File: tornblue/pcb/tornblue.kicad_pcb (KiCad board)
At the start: 2 copper layers, 152.7 x 207.8 mm, 164 parts, among them J1 BATT, J10 USB C - USB2.0, J2 SWD, J3 BREAKOUT, J4 USB C - USB2.0, J5 BATT_PIN, J6 BATT, J7 BATT_PIN, J8 BREAKOUT, J9 SWD, Q1 AO3401A, Q2 AO3401A, Q3 AO3401A, Q4 AO3401A, SW1 SW_Push, SW10 SW_Push, SW11 SW_Push, SW12 SW_Push, SW13 SW_Push, SW14 SW_Push, SW15 SW_Push, SW16 SW_Push, SW17 SW_Push, SW18 SW_Push, SW19 EC11, SW2 SW_Push, SW20 SW_Push, SW21 SW_Push, SW22 EC11, SW23 RESET, SW24 SW_SPST, SW25 SW_Push, SW26 SW_Push, SW27 SW_Push, SW28 SW_Push, SW29 SW_Push, SW3 SW_Push, SW30 SW_Push, SW31 SW_Push, SW32 SW_Push, SW33 SW_Push, SW34 SW_Push, SW35 SW_Push, SW36 SW_Push, SW37 SW_Push, SW38 SW_Push, SW39 SW_Push, SW4 SW_Push, SW40 SW_Push, SW41 SW_Push, SW42 SW_Push, SW43 EC11, SW44 SW_Push, SW45 SW_Push, SW46 EC11, SW47 SW_SPST, SW48 RESET, SW5 SW_Push, SW6 SW_Push, SW7 SW_Push, SW8 SW_Push, SW9 SW_Push, U1 XC6220, U2 TP4056, U3 nRF52840_holyiot_18010, U4 SRV05-4, U5 TP4056, U6 XC6220, U7 SRV05-4, U8 nRF52840_holyiot_18010

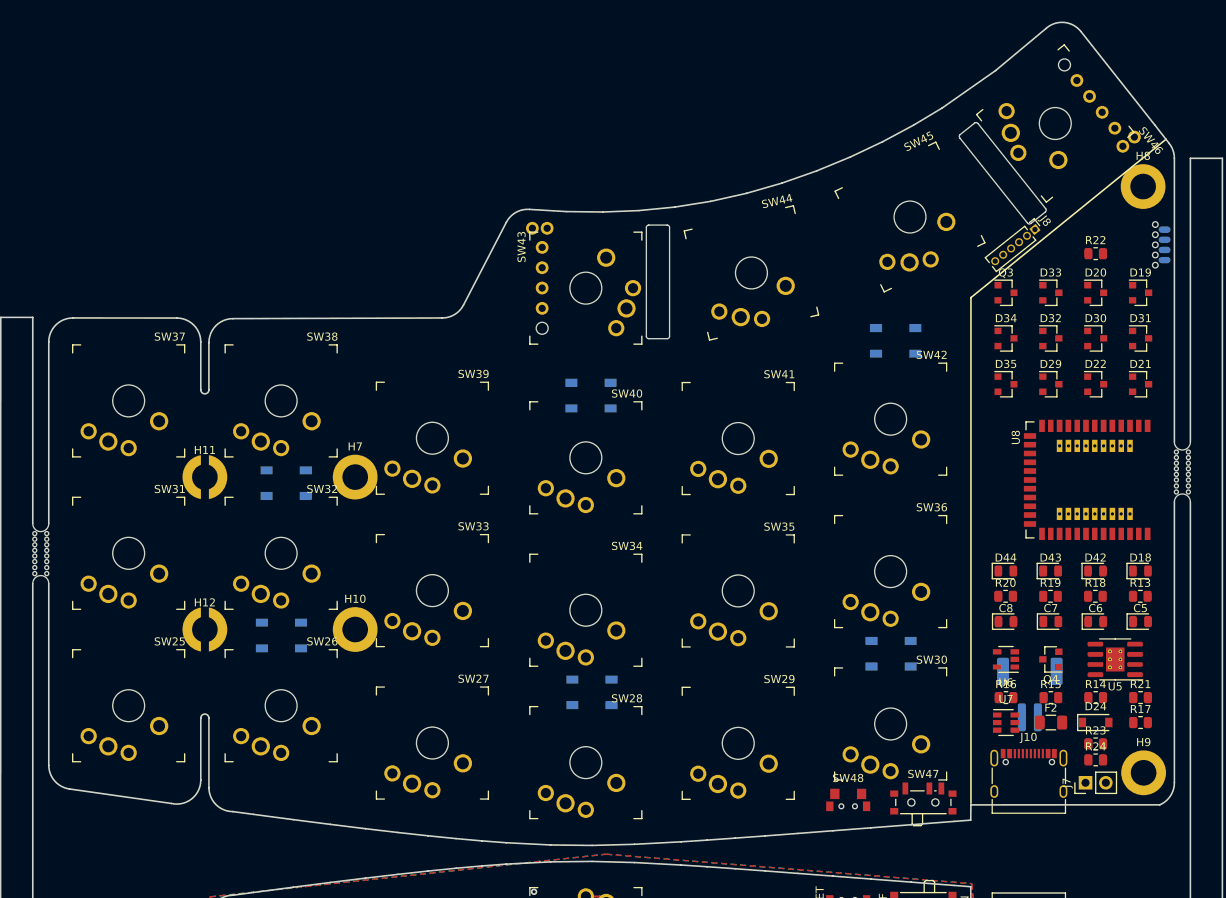
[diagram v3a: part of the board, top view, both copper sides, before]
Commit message: Add zones
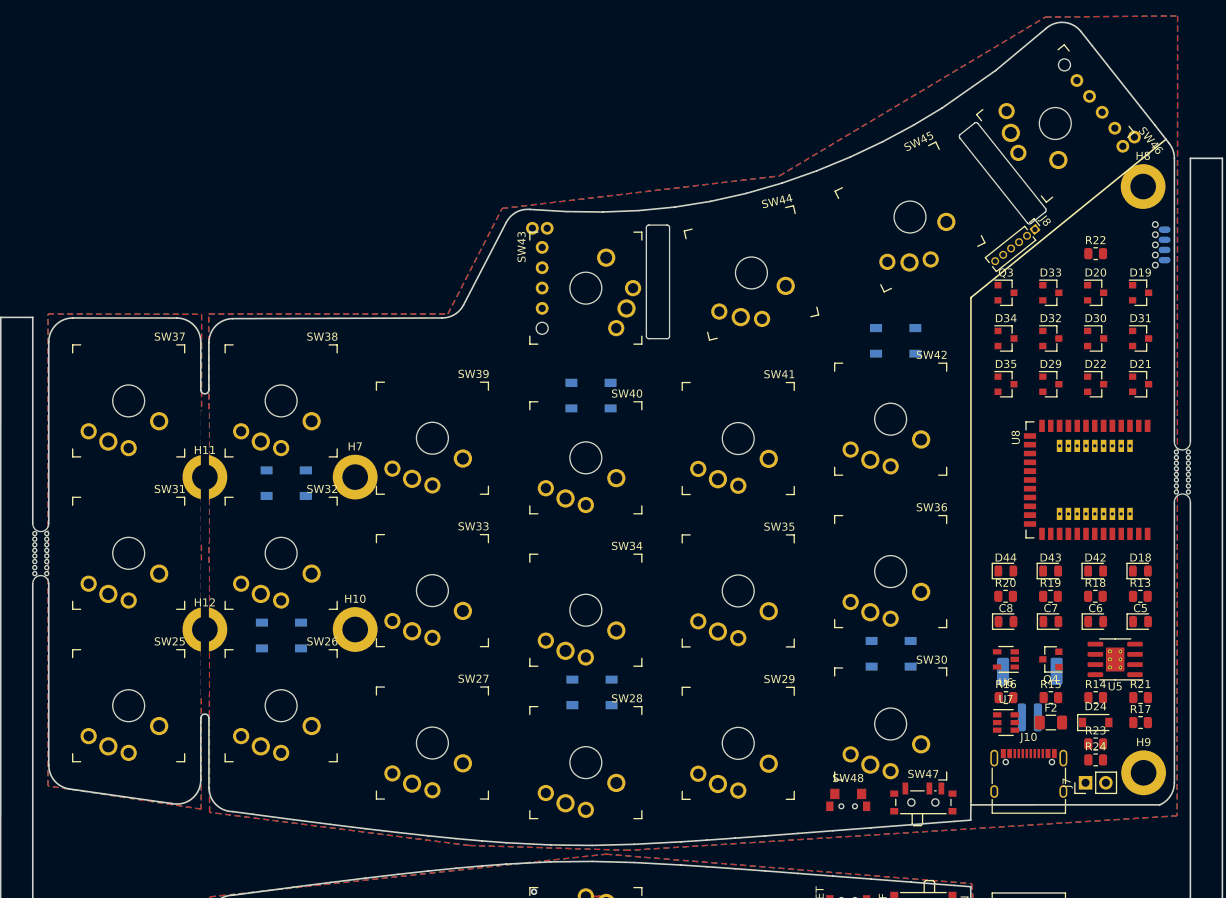
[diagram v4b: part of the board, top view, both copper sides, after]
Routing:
- added copper zone on B.Cu, net GND1
- added copper zone on F.Cu, net GND1
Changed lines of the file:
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@@
   (layers
     (0 F.Cu signal)
-    (31 B.Cu signal hide)
+    (31 B.Cu signal)
     (32 B.Adhes user hide)
     (33 F.Adhes user hide)
@@
     (38 B.Mask user hide)
     (39 F.Mask user hide)
-    (40 Dwgs.User user hide)
+    (40 Dwgs.User user)
     (41 Cmts.User user hide)
     (42 Eco1.User user hide)
     (43 Eco2.User user hide)
-    (44 Edge.Cuts user)
+    (44 Edge.Cuts user hide)
     (45 Margin user hide)
     (46 B.CrtYd user hide)
@@
     (trace_clearance 0.2)
     (zone_clearance 0.508)
-    (zone_45_only yes)
+    (zone_45_only no)
     (trace_min 0.127)
     (via_size 0.8)
@@
       )
     )
+  )
+  (zone (net 0) (net_name "") (layer F.Cu) (hatch edge 0.508)
+    (connect_pads (clearance 0.508))
+    (min_thickness 0.254)
+    (fill yes (arc_segments 32) (thermal_gap 0.508) (thermal_bridge_width 0.508))
+    (polygon
+      (pts
+        (xy 150.240979 74.549) (xy 150.1902 136.398) (xy 131.0386 133.5024) (xy 131.0386 74.5236)
+      )
+    )
+    (polygon
+      (pts
+        (xy 150.241 74.549) (xy 150.240979 74.549) (xy 150.241 74.5236)
+      )
+    )
+  )
+  (zone (net 0) (net_name "") (layer B.Cu) (hatch edge 0.508)
+    (connect_pads (clearance 0.508))
+    (min_thickness 0.254)
+    (fill yes (arc_segments 32) (thermal_gap 0.508) (thermal_bridge_width 0.508))
+    (polygon
+      (pts
+        (xy 150.240979 74.549) (xy 150.1902 136.398) (xy 131.0386 133.5024) (xy 131.0386 74.5236)
+      )
+    )
+    (polygon
+      (pts
+        (xy 150.241 74.549) (xy 150.240979 74.549) (xy 150.241 74.5236)
+      )
+    )
+  )
+  (zone (net 139) (net_name GND1) (layer F.Cu) (hatch edge 0.508)
+    (connect_pads (clearance 0.508))
+    (min_thickness 0.254)
+    (fill yes (arc_segments 32) (thermal_gap 0.508) (thermal_bridge_width 0.508))
+    (polygon
+      (pts
+        (xy 272.1864 137.2362) (xy 203.6572 141.5542) (xy 183.6674 140.9446) (xy 151.2316 136.8044) (xy 151.13 74.5236)
+        (xy 151.13 74.4982) (xy 181.0258 74.4982) (xy 187.8076 61.3156) (xy 222.4532 57.2516) (xy 255.7272 37.3888)
+        (xy 272.2372 37.2618)
+      )
+    )
+  )
+  (zone (net 139) (net_name GND1) (layer B.Cu) (hatch edge 0.508)
+    (connect_pads (clearance 0.508))
+    (min_thickness 0.254)
+    (fill yes (arc_segments 32) (thermal_gap 0.508) (thermal_bridge_width 0.508))
+    (polygon
+      (pts
+        (xy 272.1864 137.2362) (xy 203.6572 141.5542) (xy 183.6674 140.9446) (xy 151.2316 136.8044) (xy 151.13 74.5236)
+        (xy 151.13 74.4982) (xy 181.0258 74.4982) (xy 187.8076 61.3156) (xy 222.4532 57.2516) (xy 255.7272 37.3888)
+        (xy 272.2372 37.2618)
+      )
+    )
+  )
+  (zone (net 0) (net_name "") (layers F&B.Cu) (hatch edge 0.508)
+    (connect_pads (clearance 0.508))
+    (min_thickness 0.254)
+    (keepout (tracks not_allowed) (vias not_allowed) (copperpour not_allowed))
+    (fill (arc_segments 32) (thermal_gap 0.508) (thermal_bridge_width 0.508))
+    (polygon
+      (pts
+        (xy 274.1168 85.7504) (xy 274.1422 104.775) (xy 268.9606 104.7496) (xy 269.0114 85.7504) (xy 269.0114 85.725)
+      )
+    )

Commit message: Routing key matrix
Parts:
- SW43, SW46: footprint tornblue:MX_PG1350_EVQWGD001_LR_optional -> tornblue:MX_PG1350_EVQWGD001_UD_optional
- moved R17 58.9 mm to (262.0, 67.0), turned to 180 degrees
- moved R22 58.9 mm to (267.6, 125.6)
- moved Q3 46.2 mm to (256.4, 117.7)
- moved Q4 46.2 mm to (250.8, 71.9), turned to 0 degrees
- moved R21 5.63 mm to (262.0, 122.5)
- moved R14 5.61 mm to (267.6, 122.5)
- moved R23 2.00 mm to (262.0, 130.3), turned to 180 degrees
- moved R24 2.00 mm to (262.0, 128.2), turned to 180 degrees
- turned D24 to 180 degrees
- turned D36 to 180 degrees
- turned D37 to 180 degrees
- turned D38 to 180 degrees
- turned D39 to 180 degrees
- turned D40 to 180 degrees
- turned D41 to 180 degrees
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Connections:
- D19 pad 3: ROW_R0 -> ROW_R2
- D20 pad 3: ROW_R1 -> ROW_R2
- D21 pad 3: ROW_R2 -> ROW_R3
- D22 pad 3: ROW_R3 -> ROW_R0
- D31 pad 3: ROW_R2 -> ROW_R3
- D32 pad 3: ROW_R3 -> ROW_R1
- D33 pad 3: ROW_R0 -> ROW_R2
- D35 pad 3: ROW_R2 -> ROW_R0
- SW25 pad 1: COL_R2 -> COL_R0
- SW25 pad 2: Net-(D19-Pad1) -> Net-(D29-Pad1)
- SW26 pad 1: COL_R0 -> COL_R1
- SW26 pad 2: Net-(D20-Pad1) -> Net-(D35-Pad1)
- SW27 pad 1: COL_R5 -> COL_R2
- SW27 pad 2: Net-(D22-Pad1) -> Net-(D35-Pad2)
- SW28 pad 1: COL_R1 -> COL_R3
- SW28 pad 2: Net-(D35-Pad1) -> Net-(D29-Pad2)
- SW29 pad 1: COL_R1 -> COL_R4
- SW29 pad 2: Net-(D19-Pad2) -> Net-(D22-Pad2)
- SW30 pad 2: Net-(D20-Pad2) -> Net-(D21-Pad2)
- SW31 pad 1: COL_R3 -> COL_R0
- SW31 pad 2: Net-(D21-Pad2) -> Net-(D34-Pad2)
- SW32 pad 1: COL_R4 -> COL_R1
- SW32 pad 2: Net-(D22-Pad2) -> Net-(D32-Pad2)
- SW33 pad 1: COL_R3 -> COL_R2
- SW33 pad 2: Net-(D29-Pad1) -> Net-(D30-Pad2)
- SW34 pad 1: COL_R1 -> COL_R3
- SW34 pad 2: Net-(D30-Pad1) -> Net-(D31-Pad2)
- SW35 pad 1: COL_R0 -> COL_R4
- SW35 pad 2: Net-(D31-Pad1) -> Net-(D21-Pad1)
- SW36 pad 1: COL_R3 -> COL_R5
- SW36 pad 2: Net-(D32-Pad1) -> Net-(D22-Pad1)
- SW37 pad 2: Net-(D29-Pad2) -> Net-(D20-Pad2)
- SW38 pad 1: COL_R4 -> COL_R1
- SW38 pad 2: Net-(D30-Pad2) -> Net-(D19-Pad2)
- SW39 pad 1: COL_R4 -> COL_R2
- SW39 pad 2: Net-(D31-Pad2) -> Net-(D31-Pad1)
- SW40 pad 1: COL_R2 -> COL_R3
- SW40 pad 2: Net-(D32-Pad2) -> Net-(D30-Pad1)
- SW41 pad 2: Net-(D33-Pad1) -> Net-(D32-Pad1)
- SW42 pad 1: COL_R2 -> COL_R5
- SW43 pad A: ENC_RA -> ENC_RB
- SW43 pad B: ENC_RB -> ENC_RA
- SW43 pad S1: Net-(D21-Pad1) -> COL_R2
- SW43 pad S2: COL_R2 -> Net-(D33-Pad2)
- SW44 pad 1: COL_R5 -> COL_R3
- SW44 pad 2: Net-(D33-Pad2) -> Net-(D33-Pad1)
- SW45 pad 1: COL_R3 -> COL_R4
- SW45 pad 2: Net-(D34-Pad2) -> Net-(D20-Pad1)
- SW46 pad A: ENC_RA -> ENC_RB
- SW46 pad B: ENC_RB -> ENC_RA
- SW46 pad S1: Net-(D35-Pad2) -> COL_R5
- SW46 pad S2: COL_R5 -> Net-(D19-Pad1)
- U7 pad 1: USB_RD+ -> (no net)
- U7 pad 3: (no net) -> USB_RD-
- U7 pad 4: (no net) -> USB_RD+
- U7 pad 6: USB_RD- -> (no net)
- U8 pad 10: LED_R2 -> (no net)
- U8 pad 33: ROW_R2 -> (no net)
- U8 pad 34: ROW_R3 -> LED_R3
- U8 pad 35: ENC_RA -> LED_R2
- U8 pad 36: ENC_RB -> LED_R1
- U8 pad 8: LED_R1 -> (no net)
- U8 pad 9: LED_R3 -> (no net)
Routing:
- net Net-(D29-Pad1): track 0.00 -> 159.3 mm
- net Net-(D20-Pad2): track 0.00 -> 133.0 mm
- net Net-(D34-Pad2): track 0.00 -> 131.3 mm
- net Net-(D35-Pad1): track 0.00 -> 125.7 mm
- net COL_R5: track 0.00 -> 125.1 mm
- net Net-(D19-Pad2): track 0.00 -> 117.3 mm
- net Net-(D32-Pad2): track 0.00 -> 116.8 mm
- net Net-(D35-Pad2): track 0.00 -> 107.7 mm
- net COL_R4: track 0.00 -> 106.3 mm
- net Net-(D30-Pad2): track 0.00 -> 105.5 mm
- net COL_R2: track 0.00 -> 104.4 mm
- net COL_R3: track 0.00 -> 103.8 mm
- net Net-(D31-Pad1): track 0.00 -> 99.7 mm
- net Net-(D31-Pad2): track 0.00 -> 93.0 mm
- net Net-(D29-Pad2): track 0.00 -> 92.3 mm
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
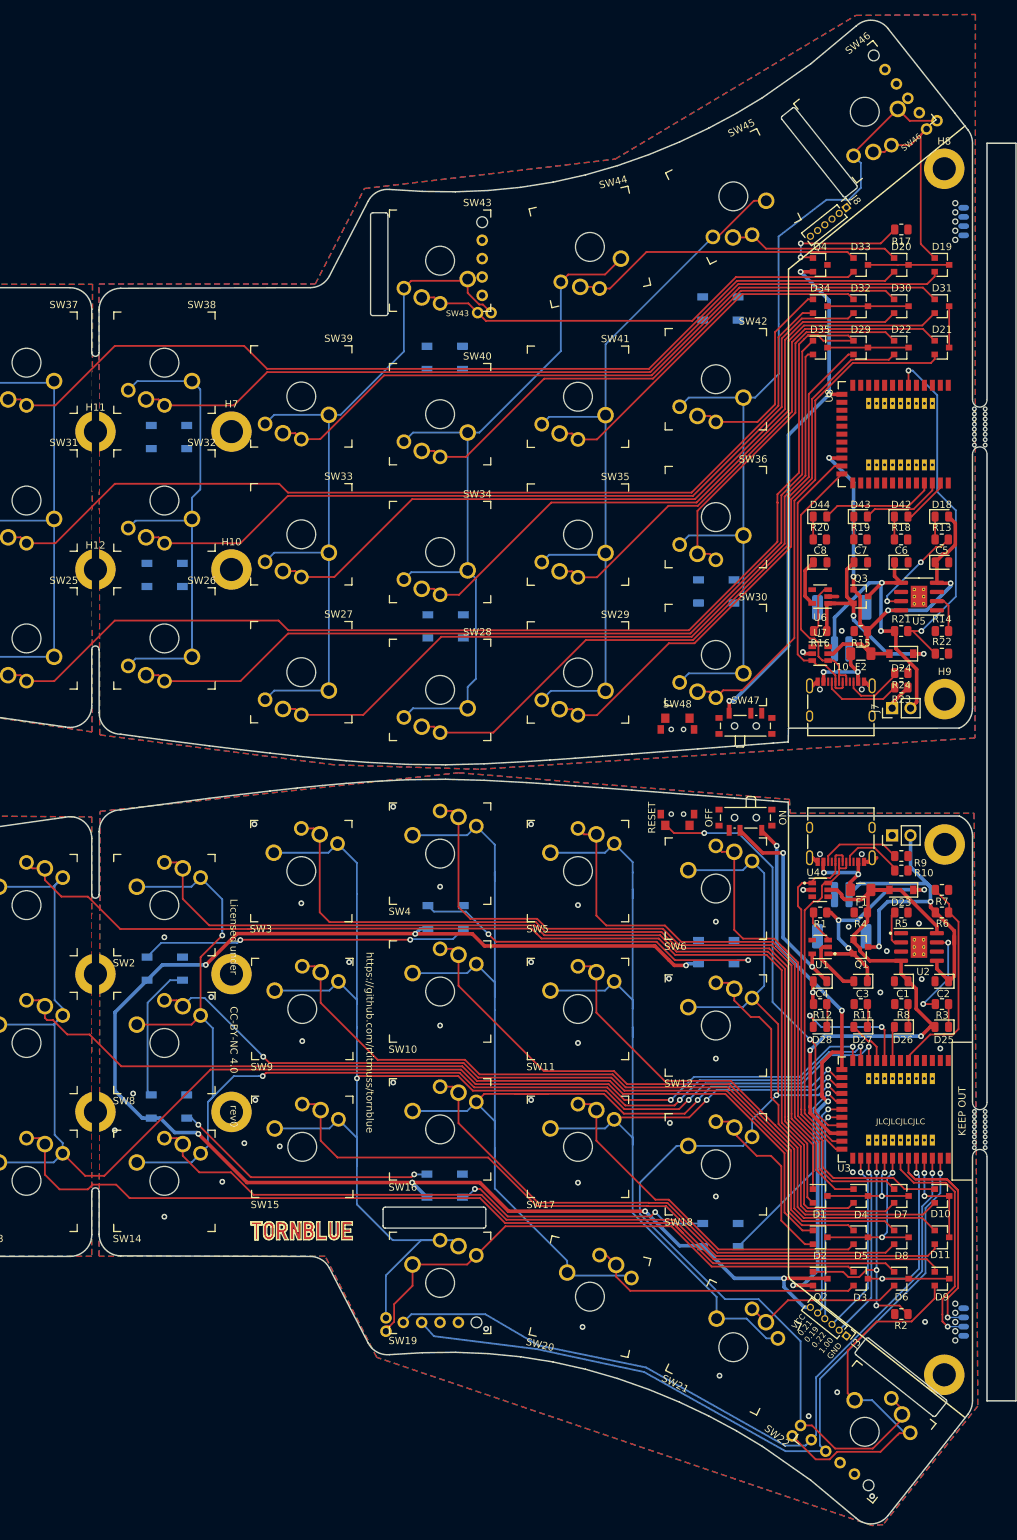
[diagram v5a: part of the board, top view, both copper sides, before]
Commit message: Finish layout, via placement and silk screen
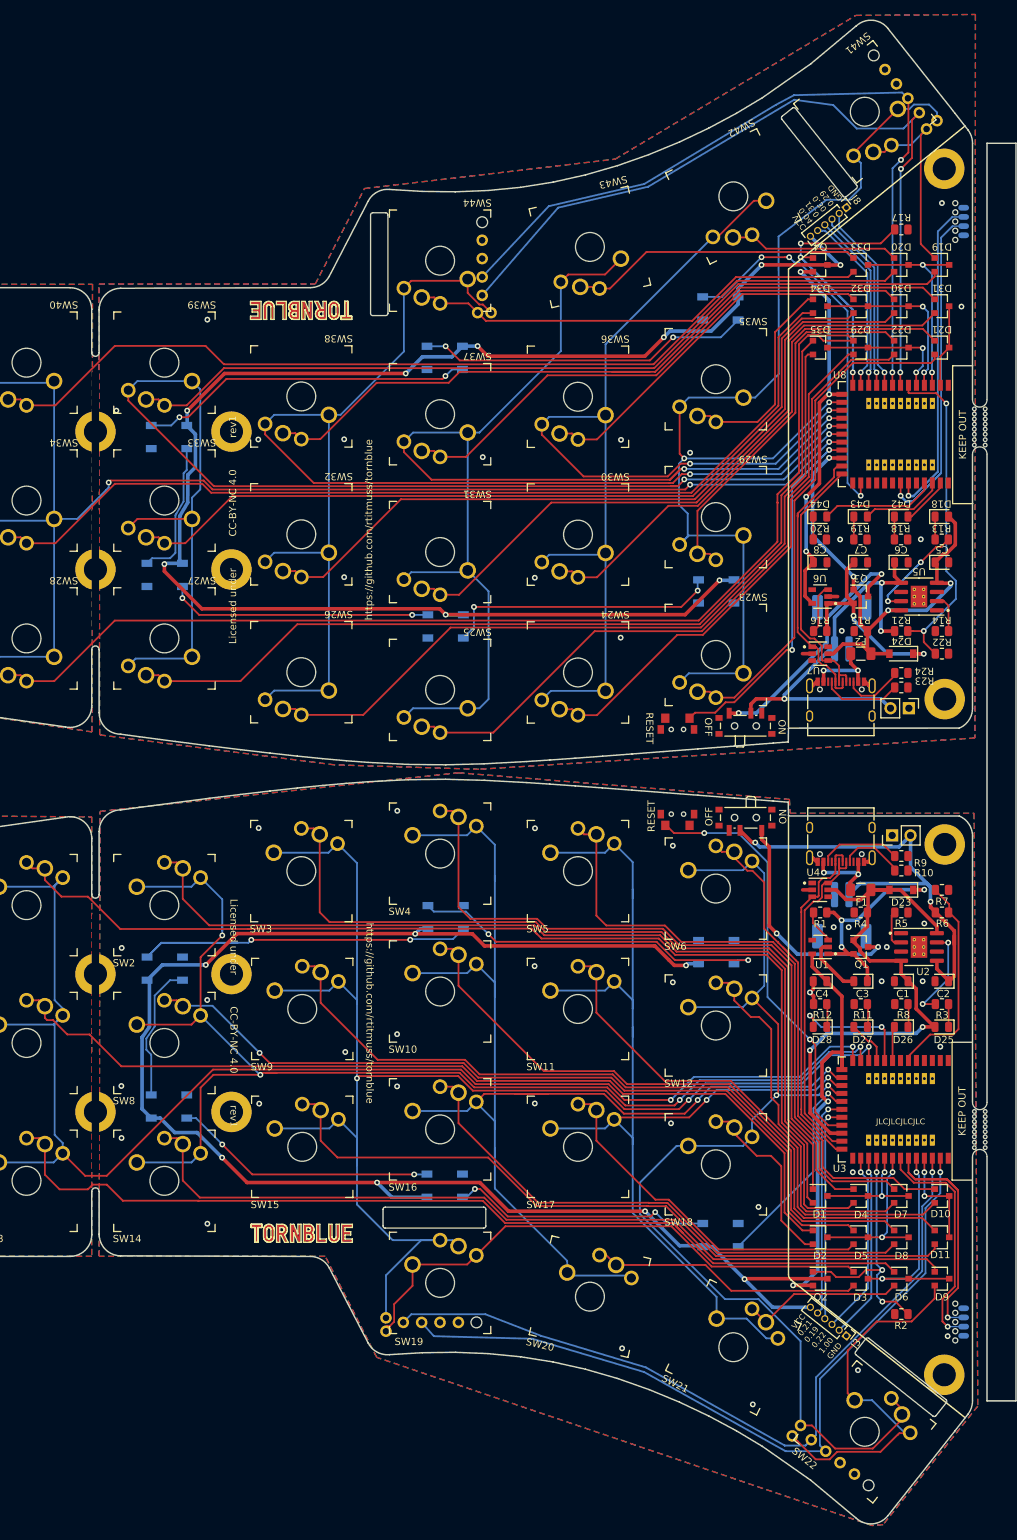
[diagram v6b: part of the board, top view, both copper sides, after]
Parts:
- moved J7 2.31 mm to (263.0, 133.1), turned to 270 degrees
- renumbered SW30 to SW23, SW29 to SW24, SW28 to SW25, SW27 to SW26, SW26 to SW27, SW25 to SW28, SW36 to SW29, SW35 to SW30, SW34 to SW31, SW33 to SW32, SW32 to SW33, SW31 to SW34, SW42 to SW35, SW41 to SW36, SW40 to SW37, SW39 to SW38, SW38 to SW39, SW37 to SW40, SW46 to SW41, SW45 to SW42, SW44 to SW43, SW43 to SW44, SW24 to SW50, SW23 to SW51, SW47 to SW52, SW48 to SW53
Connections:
- C4 pad 1: Net-(C4-Pad1) -> +3V3
- C8 pad 1: Net-(C8-Pad1) -> +3.3VP
- Q1 pad 3: VBAT -> Net-(Q1-Pad3)
- Q3 pad 3: VBAT_R -> Net-(Q3-Pad3)
- SW50 pad 1: +3V3 -> Net-(Q1-Pad3)
- SW50 pad 2: Net-(C4-Pad1) -> VBAT
- SW52 pad 1: +3.3VP -> Net-(Q3-Pad3)
- SW52 pad 2: Net-(C8-Pad1) -> VBAT_R
- U1 pad 5: Net-(C4-Pad1) -> +3V3
- U4 pad 1: USB-D+ -> (no net)
- U4 pad 3: (no net) -> USB-D+
- U6 pad 5: Net-(C8-Pad1) -> +3.3VP
- U7 pad 1: (no net) -> USB_RD-
- U7 pad 3: USB_RD- -> (no net)
- U8 pad 10: (no net) -> GPIO_RA
- U8 pad 11: COL_R2 -> GPIO_RC
- U8 pad 12: COL_R1 -> GPIO_RD
- U8 pad 13: COL_R0 -> ENABLE_R
- U8 pad 15: COL_R3 -> COL_R5
- U8 pad 17: COL_R5 -> COL_R3
- U8 pad 18: LED_RDATA -> COL_R2
- U8 pad 19: GPIO_RD -> COL_R1
- U8 pad 2: (no net) -> ROW_R3
- U8 pad 20: GPIO_RC -> COL_R0
- U8 pad 26: GPIO_RA -> LED_RDATA
- U8 pad 27: GPIO_RB -> (no net)
- U8 pad 28: ENABLE_R -> (no net)
- U8 pad 29: ROW_R0 -> (no net)
- U8 pad 3: (no net) -> ROW_R2
- U8 pad 30: ROW_R1 -> (no net)
- U8 pad 4: (no net) -> ROW_R1
- U8 pad 5: (no net) -> ROW_R0
- U8 pad 7: (no net) -> ENC_RB
- U8 pad 8: (no net) -> ENC_RA
- U8 pad 9: (no net) -> GPIO_RB
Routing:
- net EXT_R_VCC: track 0.00 -> 218.5 mm, vias 0 -> 9
- net COL_R0: track 66.1 -> 180.9 mm, vias 0 -> 3
- net ENC_RB: track 0.00 -> 111.0 mm, vias 0 -> 2
- net COL_R1: track 67.0 -> 175.9 mm, vias 0 -> 2
- net ENC_RA: track 0.00 -> 108.4 mm, vias 0 -> 2
- net COL_R2: track 104.4 -> 191.6 mm, vias 0 -> 2
- net COL_R3: track 103.8 -> 175.3 mm, vias 0 -> 2
- net Net-(SW53-Pad1): track 0.00 -> 57.1 mm, vias 0 -> 2
- net LED_RDATA: track 0.00 -> 53.8 mm, vias 0 -> 3
- net Net-(J9-Pad2): track 0.00 -> 53.3 mm, vias 0 -> 1
- net Net-(J9-Pad3): track 0.00 -> 50.4 mm, vias 0 -> 1
- net COL_R4: track 106.3 -> 155.4 mm, vias 0 -> 2
- net Net-(D37-Pad2): track 0.00 -> 46.2 mm, vias 0 -> 2
- net Net-(D36-Pad2): track 0.00 -> 46.1 mm, vias 0 -> 2
- net ENABLE_R: track 17.5 -> 56.9 mm, vias 2 -> 3
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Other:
- board text added: "0.04"
- board text added: "0.29"
- board text added: "0.30"
- board text added: "0.31"
- board text added: "Licensed under CC-BY-NC 4.0 rev1"
- board text added: "rev1 Licensed under CC-BY-NC 4.0"
- board text removed: "Licensed under CC-BY-NC 4.0 rev0"
- board text removed: "rev0 Licensed under CC-BY-NC 4.0"
